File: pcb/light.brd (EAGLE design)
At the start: 13 x 13 mm, 5 parts, among them J3 FFC3B07-05-T, U1 TEMT6000

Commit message: cleanup PCB files
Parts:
- removed JP1: (no value), adafruit_changed:1X03-CLEANBIG
- added U$1: LS_VERT, apricot:LS_VERT
- moved C1 7.05 mm to (2.79, 5.44), turned to 0 degrees
- moved J3 6.05 mm to (7.85, 11.2), turned to 180 degrees
- moved U1 4.54 mm to (7.85, 3.94), turned to 180 degrees
- moved R5 4.09 mm to (13.1, 5.44), turned to 180 degrees
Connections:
- net +3V3: now also U$1.B1, U$1.B2; no longer JP1.1
- net GND: now also U$1.T1, U$1.T2; no longer JP1.2
- net S: now also U$1.B3, U$1.B4, U$1.T3, U$1.T4; no longer JP1.3
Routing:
- net GND: track 0.00 -> 6.78 mm, vias 2 -> 4
- net S: track 9.12 -> 14.4 mm, vias 0 -> 2
- net +3V3: track 17.1 -> 20.3 mm, vias 0 -> 2
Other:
- board size 13 x 13 mm -> 15.7 x 15.2 mm
- board text added: "PulseHPT.com"
- board text removed: "G"
- board text removed: "PulseHPT.com dekuNukem 2023"
- board text removed: "S"
- board text removed: "V"

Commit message: photodiode
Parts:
- removed U1: TEMT6000, SparkFun:TEMT6000-SEN
- added D1: BPW_34_S-Z, BPW_34_S-Z:DIO_BPW_34_S-Z
- added U$5: TLV2371DBV, texas-instruments:SOT23-5L
- C1: value 100nF -> DNP
- R5: value 10K -> 51K?
- moved C1 11.9 mm to (14.7, 5.59), turned to 90 degrees
- moved J3 1.65 mm to (7.85, 12.8)
- moved R5 0.15 mm to (13.1, 5.59), turned to 90 degrees
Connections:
- removed net S: J3.3, R5.2, U$1.B3, U$1.B4, U$1.T3, U$1.T4, U1.EMITTER
- new net LS_SIGNAL: C1.1, J3.3, R5.1, U$1.B3, U$1.B4, U$1.T3, U$1.T4, U$5.1
- new net N$2: C1.2, D1.C, R5.2, U$5.4
- net +3V3: now also U$5.5; no longer C1.2, U1.COLLECTOR
- net GND: now also D1.A, U$5.2, U$5.3; no longer C1.1, R5.1
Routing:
- net LS_SIGNAL: track 0.00 -> 32.3 mm, vias 0 -> 2
- net S: track 14.4 -> 0.00 mm, vias 2 -> 0
- net N$2: track 0.00 -> 12.8 mm
- net GND: track 6.78 -> 5.00 mm, vias 4 -> 6
- net +3V3: track 20.3 -> 21.5 mm, vias 2 -> 1
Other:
- board size 15.7 x 15.2 mm -> 15.7 x 16.8 mm

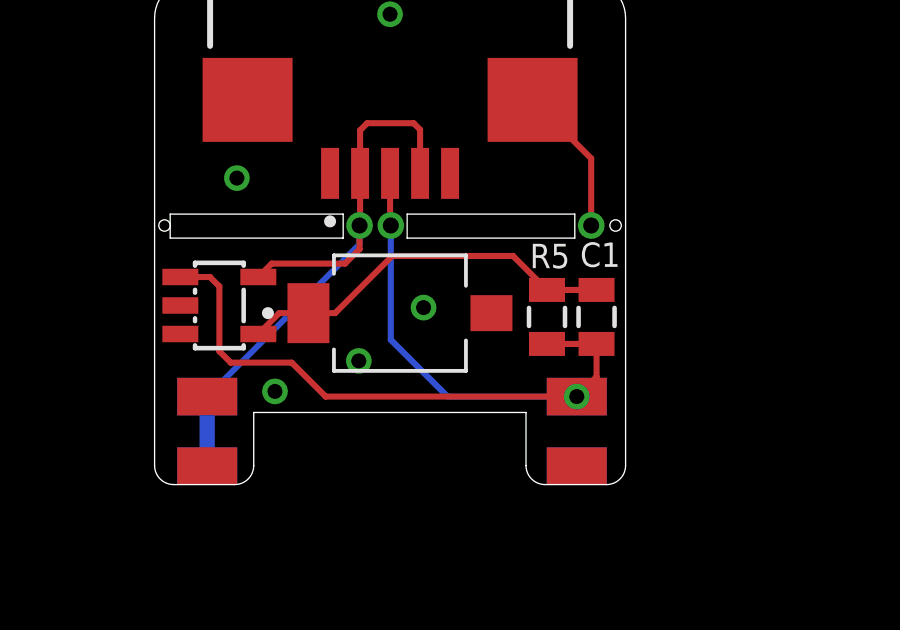
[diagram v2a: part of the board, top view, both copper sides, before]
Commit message: adjusted resistor
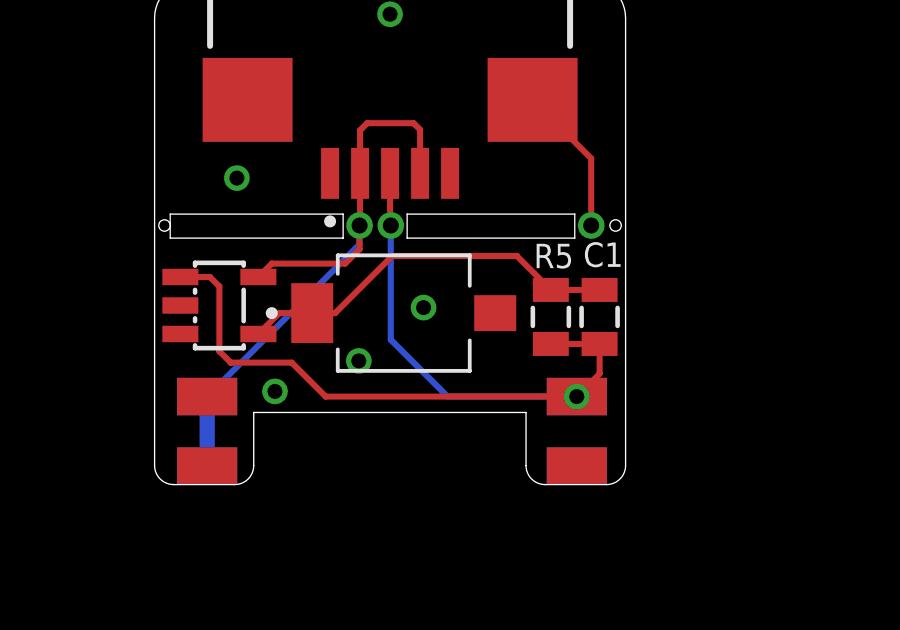
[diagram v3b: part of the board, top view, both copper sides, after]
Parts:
- moved R5 0.13 mm to (13.2, 5.59)
- moved D1 0.13 mm to (8.31, 5.71)
- moved C1 0.10 mm to (14.8, 5.59)
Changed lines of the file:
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@@
 <attribute name="SNAPEDA_LINK" value="https://www.snapeda.com/parts/FFC3B07-05-T/Global+Connector+Technology/view-part/?ref=snap" x="7.85" y="12.823" size="1.778" layer="27" rot="R180" display="off"/>
 </element>
-<element name="R5" library="joyAnalog" package="0805" value="51K?" x="13.081" y="5.588" smashed="yes" rot="R90">
-<attribute name="NAME" x="12.5094" y="7.2136" size="0.8128" layer="25"/>
+<element name="R5" library="joyAnalog" package="0805" value="51K?" x="13.208" y="5.588" smashed="yes" rot="R90">
+<attribute name="NAME" x="12.6364" y="7.2136" size="0.8128" layer="25"/>
 </element>
-<element name="C1" library="clock" package="0805" value="DNP" x="14.732" y="5.588" smashed="yes" rot="R90">
-<attribute name="NAME" x="14.185" y="7.2565" size="0.8128" layer="25"/>
+<element name="C1" library="clock" package="0805" value="DNP" x="14.8336" y="5.588" smashed="yes" rot="R90">
+<attribute name="NAME" x="14.2866" y="7.2565" size="0.8128" layer="25"/>
 </element>
 <element name="U$1" library="apricot" package="LS_VERT" value="LS_VERT" x="7.85" y="1.174" smashed="yes" rot="R90"/>
 <element name="U$5" library="texas-instruments" package="SOT23-5L" value="TLV2371DBV" x="2.159" y="5.969" smashed="yes" rot="R270"/>
-<element name="D1" library="BPW_34_S-Z" package="DIO_BPW_34_S-Z" value="BPW_34_S-Z" x="8.1788" y="5.715" smashed="yes" rot="R180">
-<attribute name="AVAILABILITY" value="In Stock" x="8.1788" y="5.715" size="1.778" layer="27" rot="R180" display="off"/>
-<attribute name="CHECK_PRICES" value="https://www.snapeda.com/parts/BPW%2034%20S-Z/OSRAM/view-part/?ref=eda" x="8.1788" y="5.715" size="1.778" layer="27" rot="R180" display="off"/>
-<attribute name="DESCRIPTION" value="                                                      Photodiode 850nm 20ns 120° 2-SMD, Gull Wing                                              " x="8.1788" y="5.715" size="1.778" layer="27" rot="R180" display="off"/>
-<attribute name="MF" value="OSRAM Opto" x="8.1788" y="5.715" size="1.778" layer="27" rot="R180" display="off"/>
-<attribute name="MP" value="BPW 34 S-Z" x="8.1788" y="5.715" size="1.778" layer="27" rot="R180" display="off"/>
-<attribute name="PACKAGE" value="SMD-2 OSRAM Opto Semiconductors" x="8.1788" y="5.715" size="1.778" layer="27" rot="R180" display="off"/>
-<attribute name="PRICE" value="None" x="8.1788" y="5.715" size="1.778" layer="27" rot="R180" display="off"/>
-<attribute name="SNAPEDA_LINK" value="https://www.snapeda.com/parts/BPW%2034%20S-Z/OSRAM/view-part/?ref=snap" x="8.1788" y="5.715" size="1.778" layer="27" rot="R180" display="off"/>
+<element name="D1" library="BPW_34_S-Z" package="DIO_BPW_34_S-Z" value="BPW_34_S-Z" x="8.3058" y="5.715" smashed="yes" rot="R180">
+<attribute name="AVAILABILITY" value="In Stock" x="8.3058" y="5.715" size="1.778" layer="27" rot="R180" display="off"/>
+<attribute name="CHECK_PRICES" value="https://www.snapeda.com/parts/BPW%2034%20S-Z/OSRAM/view-part/?ref=eda" x="8.3058" y="5.715" size="1.778" layer="27" rot="R180" display="off"/>
+<attribute name="DESCRIPTION" value="                                                      Photodiode 850nm 20ns 120° 2-SMD, Gull Wing                                              " x="8.3058" y="5.715" size="1.778" layer="27" rot="R180" display="off"/>
+<attribute name="MF" value="OSRAM Opto" x="8.3058" y="5.715" size="1.778" layer="27" rot="R180" display="off"/>
+<attribute name="MP" value="BPW 34 S-Z" x="8.3058" y="5.715" size="1.778" layer="27" rot="R180" display="off"/>
+<attribute name="PACKAGE" value="SMD-2 OSRAM Opto Semiconductors" x="8.3058" y="5.715" size="1.778" layer="27" rot="R180" display="off"/>
+<attribute name="PRICE" value="None" x="8.3058" y="5.715" size="1.778" layer="27" rot="R180" display="off"/>
+<attribute name="SNAPEDA_LINK" value="https://www.snapeda.com/parts/BPW%2034%20S-Z/OSRAM/view-part/?ref=snap" x="8.3058" y="5.715" size="1.778" layer="27" rot="R180" display="off"/>
 </element>
 </elements>
@@
 <wire x1="5.703" y1="2.933" x2="14.073" y2="2.933" width="0.2032" layer="1"/>
 <wire x1="4.572" y1="4.064" x2="5.703" y2="2.933" width="0.2032" layer="1"/>
-<wire x1="14.073" y1="2.933" x2="14.732" y2="3.592" width="0.2032" layer="1"/>
-<wire x1="14.732" y1="3.592" x2="14.732" y2="4.688" width="0.2032" layer="1"/>
-<wire x1="14.732" y1="4.688" x2="13.081" y2="4.688" width="0.2032" layer="1"/>
+<wire x1="14.8336" y1="4.688" x2="13.208" y2="4.688" width="0.2032" layer="1"/>
 <wire x1="7.874" y1="8.636" x2="7.874" y2="4.826" width="0.2032" layer="16"/>
 <wire x1="9.767" y1="2.933" x2="14.073" y2="2.933" width="0.2032" layer="16"/>
@@
 <wire x1="2.159" y1="6.604" x2="2.159" y2="4.445" width="0.2032" layer="1"/>
 <wire x1="2.159" y1="4.445" x2="2.54" y2="4.064" width="0.2032" layer="1"/>
+<wire x1="14.8336" y1="4.688" x2="14.8336" y2="3.6936" width="0.2032" layer="1"/>
+<wire x1="14.8336" y1="3.6936" x2="14.073" y2="2.933" width="0.2032" layer="1"/>
 <wire x1="14.073" y1="0.6168" x2="14.073" y2="0.6168" width="0" layer="19" extent="1-16"/>
 <wire x1="14.073" y1="2.933" x2="14.073" y2="0.6168" width="0" layer="19" extent="16-16"/>
@@
 <contactref element="C1" pad="2"/>
 <wire x1="7.9228" y1="7.62" x2="6.0178" y2="5.715" width="0.2032" layer="1"/>
-<wire x1="5.1288" y1="5.715" x2="6.0178" y2="5.715" width="0.2032" layer="1"/>
-<wire x1="11.949" y1="7.62" x2="13.081" y2="6.488" width="0.2032" layer="1"/>
-<wire x1="7.9228" y1="7.62" x2="11.949" y2="7.62" width="0.2032" layer="1"/>
-<wire x1="13.081" y1="6.488" x2="14.732" y2="6.488" width="0.2032" layer="1"/>
+<wire x1="5.2558" y1="5.715" x2="6.0178" y2="5.715" width="0.2032" layer="1"/>
+<wire x1="12.076" y1="7.62" x2="13.208" y2="6.488" width="0.2032" layer="1"/>
+<wire x1="7.9228" y1="7.62" x2="12.076" y2="7.62" width="0.2032" layer="1"/>
+<wire x1="13.208" y1="6.488" x2="14.8336" y2="6.488" width="0.2032" layer="1"/>
 <wire x1="3.459" y1="5.019" x2="4.155" y2="5.715" width="0.2032" layer="1"/>
-<wire x1="4.155" y1="5.715" x2="5.1288" y2="5.715" width="0.2032" layer="1"/>
+<wire x1="4.155" y1="5.715" x2="5.2558" y2="5.715" width="0.2032" layer="1"/>
 </signal>
 </signals>

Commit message: adjusted gain resistor values, added more captures
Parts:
- R5: value 51K? -> 68K
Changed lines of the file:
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@@
 <attribute name="SNAPEDA_LINK" value="https://www.snapeda.com/parts/FFC3B07-05-T/Global+Connector+Technology/view-part/?ref=snap" x="7.85" y="12.823" size="1.778" layer="27" rot="R180" display="off"/>
 </element>
-<element name="R5" library="joyAnalog" package="0805" value="51K?" x="13.208" y="5.588" smashed="yes" rot="R90">
+<element name="R5" library="joyAnalog" package="0805" value="68K" x="13.208" y="5.588" smashed="yes" rot="R90">
 <attribute name="NAME" x="12.6364" y="7.2136" size="0.8128" layer="25"/>
 </element>
